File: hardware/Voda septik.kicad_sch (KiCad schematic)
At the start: 39 parts, among them J1 Screw_Terminal_01x09, J2 RS-485 elektroměr, J3 Display TM1637, J4 Display LCD I2C, U1 ESP32-DevKitC, U2 DC-DC 24V -> 5V, U4 MAX3485-modul

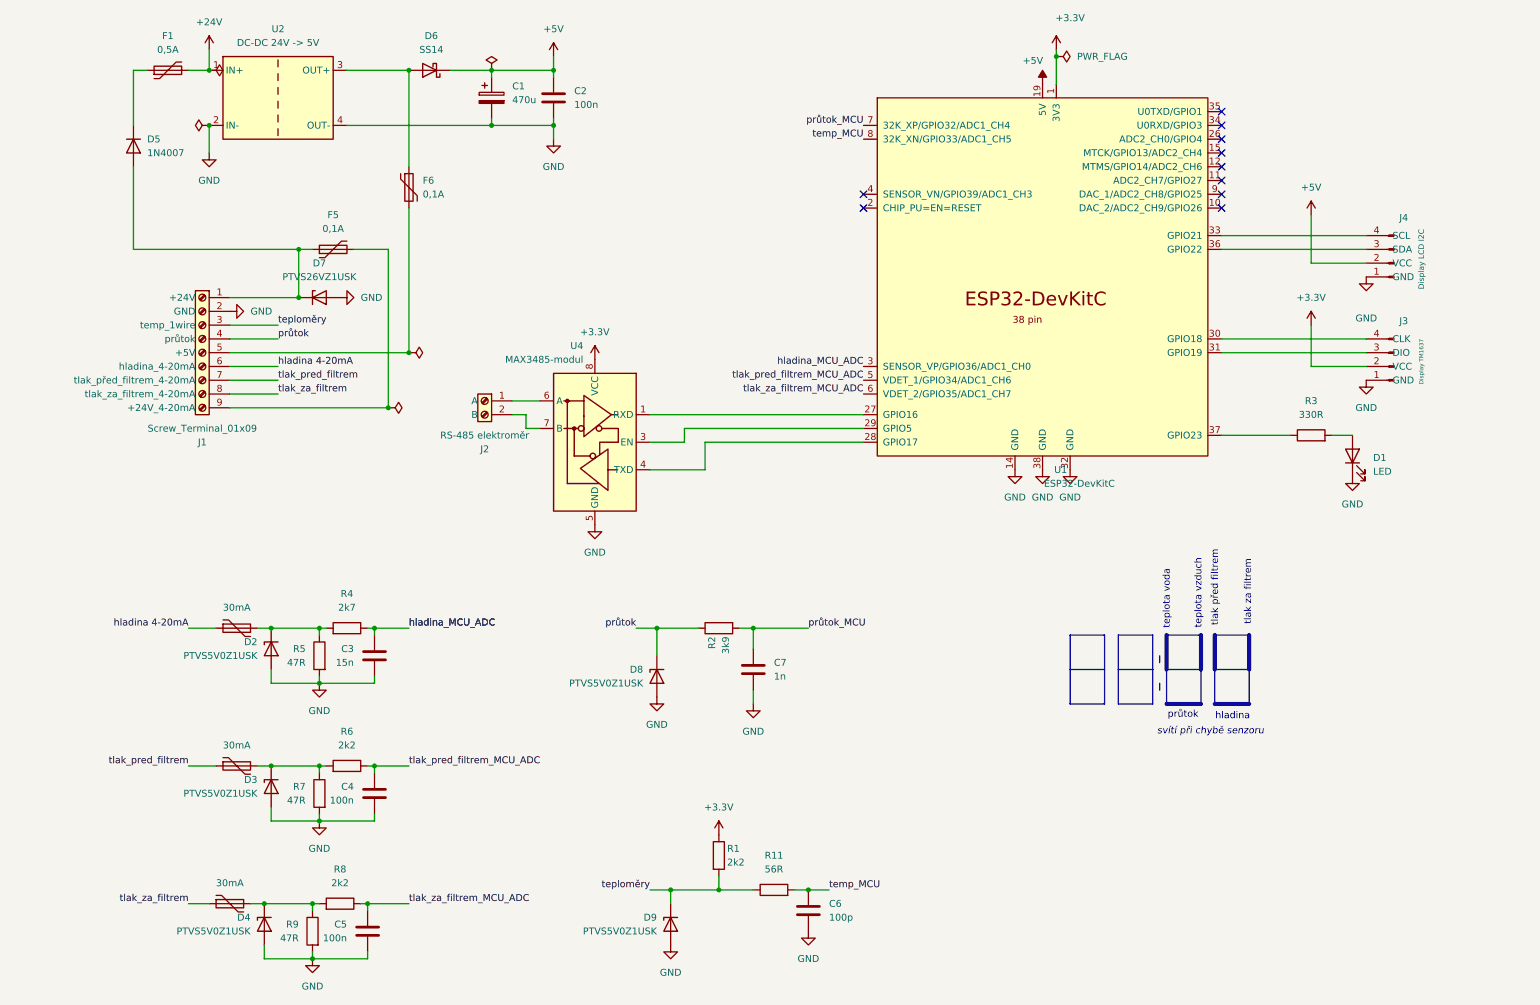
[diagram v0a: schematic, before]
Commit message: Dokončení schématu a návrhu PCB o stavu, který byl poslán do výroby.
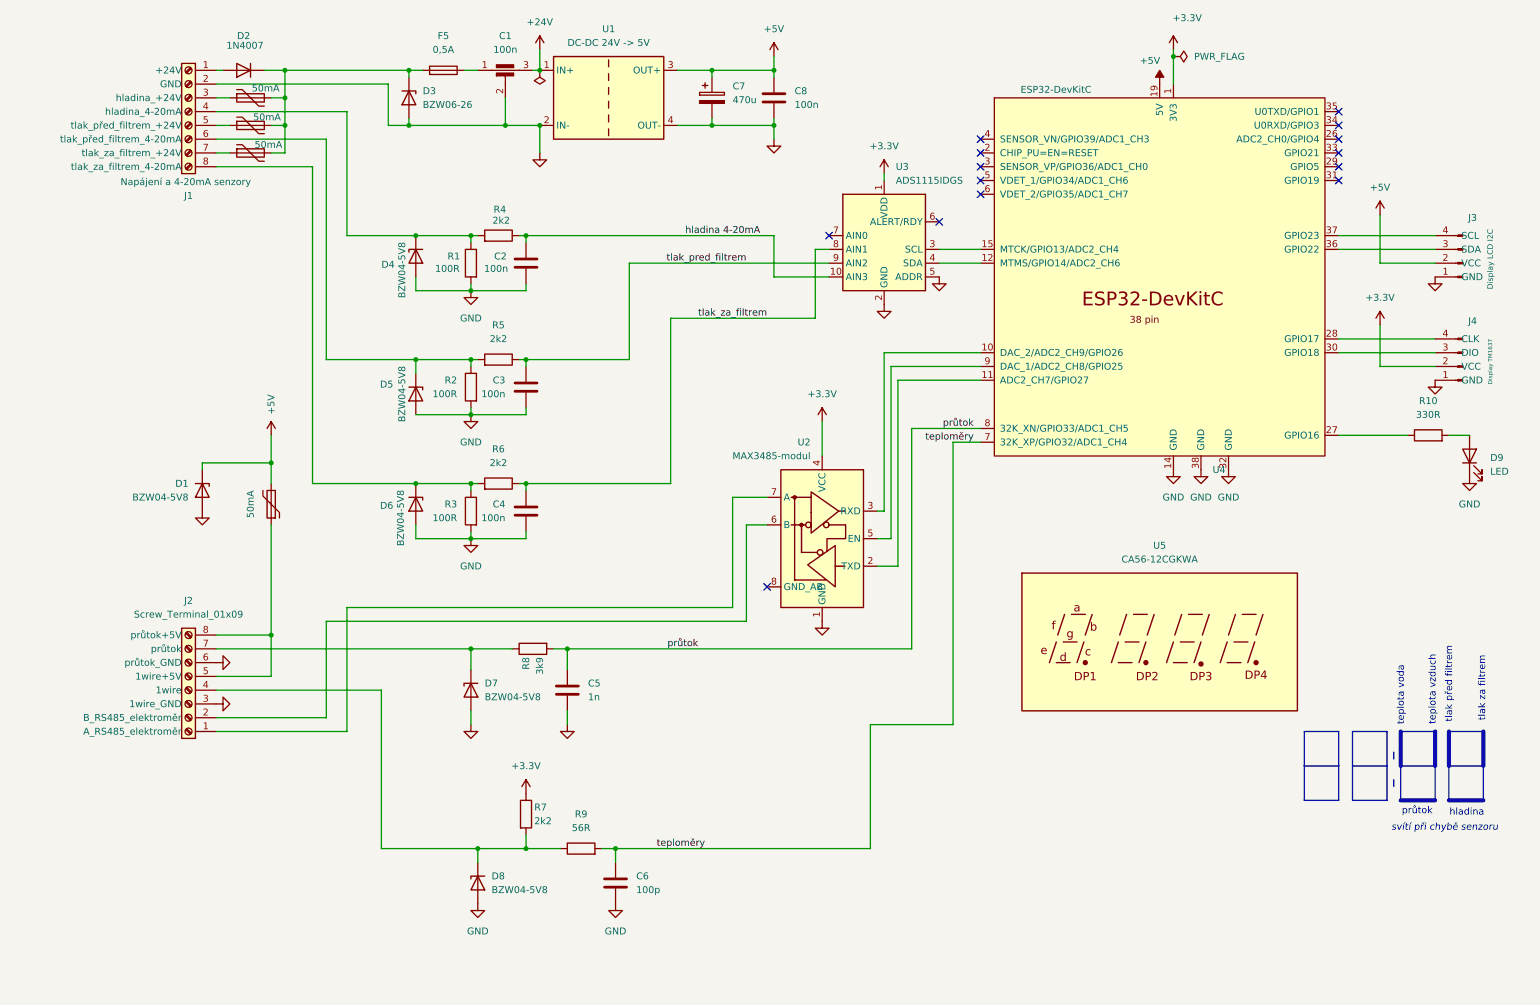
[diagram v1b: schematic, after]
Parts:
- removed D3, D4: PTVS5V0Z1USK, Diode_SMD:Nexperia_DSN1608-2_1.6x0.8mm, symbol Diode:PTVS5V0Z1USK
- removed D6: SS14, symbol Device:D_Schottky
- removed F6: 0,1A, symbol Device:Polyfuse
- removed J2: RS-485 elektroměr, TerminalBlock_RND:TerminalBlock_RND_205-00001_1x02_P5.00mm_Horizontal, symbol Connector:Screw_Terminal_01x02
- added C1: 100n, martin:Odruseni_3x_2.54mm, symbol Device:Filter_EMI_C
- added D1, D5, D6: BZW04-5V8, Diode_THT:D_DO-15_P2.54mm_Vertical_AnodeUp, symbol martin:BZW04-5V8
- added J2: Screw_Terminal_01x09, martin:Svorky_EB147A_8_5.08, symbol Connector:Screw_Terminal_01x09
- added U3: ADS1115IDGS, martin:ADS1115_modul_vertical, symbol Analog_ADC:ADS1115IDGS
- added U5: CA56-12CGKWA, martin:DISPLAY_clok_MOUNT_4xM3, symbol Display_Character:CA56-12CGKWA
- C2: renamed from C3; value 15n -> 100n; footprint (none) -> Capacitor_THT:C_Disc_D5.0mm_W2.5mm_P5.00mm
- C3: renamed from C4; footprint (none) -> Capacitor_THT:C_Disc_D5.0mm_W2.5mm_P5.00mm
- C4: renamed from C5; footprint (none) -> Capacitor_THT:C_Disc_D5.0mm_W2.5mm_P5.00mm
- C5: renamed from C7; footprint (none) -> Capacitor_THT:C_Disc_D5.0mm_W2.5mm_P5.00mm
- C6: footprint (none) -> Capacitor_THT:C_Disc_D5.0mm_W2.5mm_P5.00mm
- C7: renamed from C1; footprint (none) -> Capacitor_THT:CP_Radial_D10.0mm_P5.00mm
- C8: renamed from C2; footprint (none) -> Capacitor_THT:C_Disc_D5.0mm_W2.5mm_P5.00mm
- D2: renamed from D5; footprint Diode_THT:D_DO-41_SOD81_P10.16mm_Horizontal -> Diode_THT:D_DO-15_P2.54mm_Vertical_AnodeUp
- D3: renamed from D7; value PTVS26VZ1USK -> BZW06-26; footprint Diode_SMD:Nexperia_DSN1608-2_1.6x0.8mm -> Diode_THT:D_DO-15_P2.54mm_Vertical_AnodeUp; symbol Diode:PTVS26VZ1USK -> martin:BZW06-26
- D4: renamed from D2; value PTVS5V0Z1USK -> BZW04-5V8; footprint Diode_SMD:Nexperia_DSN1608-2_1.6x0.8mm -> Diode_THT:D_DO-15_P2.54mm_Vertical_AnodeUp; symbol Diode:PTVS5V0Z1USK -> martin:BZW04-5V8
- D7: renamed from D8; value PTVS5V0Z1USK -> BZW04-5V8; footprint Diode_SMD:Nexperia_DSN1608-2_1.6x0.8mm -> Diode_THT:D_DO-15_P2.54mm_Vertical_AnodeUp; symbol Diode:PTVS5V0Z1USK -> martin:BZW04-5V8
- D8: renamed from D9; value PTVS5V0Z1USK -> BZW04-5V8; footprint Diode_SMD:Nexperia_DSN1608-2_1.6x0.8mm -> Diode_THT:D_DO-15_P2.54mm_Vertical_AnodeUp; symbol Diode:PTVS5V0Z1USK -> martin:BZW04-5V8
- D9: renamed from D1; footprint (none) -> LED_THT:LED_D3.0mm
- F1: renamed from F2; value 30mA -> 50mA; footprint (none) -> martin:Fuse_Disc_D8.3_W3.8_P5.1
- F2: renamed from F3; value 30mA -> 50mA; footprint (none) -> martin:Fuse_Disc_D8.3_W3.8_P5.1
- F3: renamed from F4; value 30mA -> 50mA; footprint (none) -> martin:Fuse_Disc_D8.3_W3.8_P5.1
- F4: renamed from F5; value 0,1A -> 50mA; footprint (none) -> martin:Fuse_Disc_D8.3_W3.8_P5.1
- F5: renamed from F1; footprint (none) -> martin:Fuse_Axial_L11mm_D3.9mm_P15.24mm_Horizontal
- J1: value Screw_Terminal_01x09 -> Napájení a 4-20mA senzory; footprint TerminalBlock_Phoenix:TerminalBlock_Phoenix_MKDS-1,5-9_1x09_P5.00mm_Horizontal -> martin:Svorky_EB147A_8_5.08
- J3: renamed from J4; footprint (none) -> Connector_PinHeader_2.54mm:PinHeader_1x04_P2.54mm_Vertical
- J4: renamed from J3; footprint (none) -> Connector_PinHeader_2.54mm:PinHeader_1x04_P2.54mm_Vertical
- R1: renamed from R5; value 47R -> 100R; footprint (none) -> Resistor_THT:R_Axial_DIN0207_L6.3mm_D2.5mm_P2.54mm_Vertical
- R10: renamed from R3; footprint (none) -> Resistor_THT:R_Axial_DIN0207_L6.3mm_D2.5mm_P2.54mm_Vertical
- R2: renamed from R7; value 47R -> 100R; footprint (none) -> Resistor_THT:R_Axial_DIN0207_L6.3mm_D2.5mm_P2.54mm_Vertical
- R3: renamed from R9; value 47R -> 100R; footprint (none) -> Resistor_THT:R_Axial_DIN0207_L6.3mm_D2.5mm_P2.54mm_Vertical
- R4: value 2k7 -> 2k2; footprint (none) -> Resistor_THT:R_Axial_DIN0207_L6.3mm_D2.5mm_P2.54mm_Vertical
- R5: renamed from R6; footprint (none) -> Resistor_THT:R_Axial_DIN0207_L6.3mm_D2.5mm_P2.54mm_Vertical
- R6: renamed from R8; footprint (none) -> Resistor_THT:R_Axial_DIN0207_L6.3mm_D2.5mm_P2.54mm_Vertical
- R7: renamed from R1; footprint (none) -> Resistor_THT:R_Axial_DIN0207_L6.3mm_D2.5mm_P2.54mm_Vertical
- R8: renamed from R2; footprint (none) -> Resistor_THT:R_Axial_DIN0207_L6.3mm_D2.5mm_P2.54mm_Vertical
- R9: renamed from R11; footprint (none) -> Resistor_THT:R_Axial_DIN0207_L6.3mm_D2.5mm_P2.54mm_Vertical
- U1: renamed from U2; footprint Converter_DCDC:Converter_DCDC_Murata_CRE1xxxxxxDC_THT -> martin:LM2596 DC-DC HW-411
- U2: renamed from U4; footprint (none) -> martin:MAX3485-modul
- renumbered U1 to U4
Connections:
- net +24V: now also C1.3; no longer F5.2
- net +3.3V: now also U2.4 (VCC), U3.1 (VDD); no longer U2.8 (VCC)
- net +5V: now also F4.2, U1.3 (OUT+), D1.1 (K)
- net GND: now also U2.1 (GND), C1.2, D1.2 (A), D5.2 (A), D6.2 (A), J2.3 (1wire_GND), J2.6 (průtok_GND), U3.2 (GND), U3.5 (ADDR); no longer U2.5 (GND)
- net hladina 4-20mA: now also C2.1, R4.1, U3.10 (AIN3); no longer F1.1, J1.6 (hladina_4-20mA)
- net průtok: now also C5.1, R8.2, U4.8 (32K_XN/GPIO33/ADC1_CH5); no longer D7.1 (K), J1.4 (průtok), R8.1
- net teploměry: now also C6.1, R9.2, U4.7 (32K_XP/GPIO32/ADC1_CH4); no longer D8.1 (K), J1.3 (temp_1wire), R7.2, R9.1
- net tlak_pred_filtrem: now also C3.1, R5.1, U3.9 (AIN2); no longer F2.1, J1.7 (tlak_před_filtrem_4-20mA)
- net tlak_za_filtrem: now also C4.1, R6.1, U3.8 (AIN1); no longer F3.1, J1.8 (tlak_za_filtrem_4-20mA)
- net at D2.1 (K), F5.1: now also D3.1 (K), F1.2, F2.2, F3.2
- net at R2.1, R5.2: now also J1.6 (tlak_před_filtrem_4-20mA), D5.1 (K); no longer F2.2
- net at R10.1: now also U4.27 (GPIO16); no longer U4.37 (GPIO23)
- net at D4.1 (K), R1.1, R4.2: now also J1.4 (hladina_4-20mA); no longer F1.2
- net at J4.3 (DIO): now also U4.30 (GPIO18); no longer U4.31 (GPIO19)
- net at J4.4 (CLK): now also U4.28 (GPIO17); no longer U4.30 (GPIO18)
- net at J1.5 (tlak_před_filtrem_+24V): now also F2.1
- net at U2.3 (RXD): now also U4.10 (DAC_2/ADC2_CH9/GPIO26); no longer U4.29 (GPIO5)
- net at U2.6 (B): now also J2.2 (B_RS485_elektroměr)
- net at U2.7 (A): now also J2.1 (A_RS485_elektroměr)
- net at R3.1, R6.2: now also J1.8 (tlak_za_filtrem_4-20mA), D6.1 (K); no longer F3.2
- net at U4.11 (ADC2_CH7/GPIO27): now also U2.2 (TXD)
- net at U4.12 (MTMS/GPIO14/ADC2_CH6): now also U3.4 (SDA)
- net at U4.15 (MTCK/GPIO13/ADC2_CH4): now also U3.3 (SCL)
- net at U4.33 (GPIO21): no longer J3.4 (SCL)
- net at U4.9 (DAC_1/ADC2_CH8/GPIO25): now also U2.5 (EN)
- net at D2.2 (A), J1.1 (+24V): no longer D3.1 (K), F4.1
- removed net hladina_MCU_ADC: C2.1, R4.1, U4.3 (SENSOR_VP/GPIO36/ADC1_CH0)
- removed net průtok_MCU: C5.1, R8.2, U4.7 (32K_XP/GPIO32/ADC1_CH4)
- removed net temp_MCU: C6.1, R9.2, U4.8 (32K_XN/GPIO33/ADC1_CH5)
- removed net tlak_pred_filtrem_MCU_ADC: C3.1, R5.1, U4.5 (VDET_1/GPIO34/ADC1_CH6)
- removed net tlak_za_filtrem_MCU_ADC: C4.1, R6.1, U4.6 (VDET_2/GPIO35/ADC1_CH7)
- new net: C1.1, F5.2
- new net: D8.1 (K), J2.4 (1wire), R7.2, R9.1
- new net: D7.1 (K), J2.7 (průtok), R8.1
- new net: F3.1, J1.7 (tlak_za_filtrem_+24V)
- new net: J3.4 (SCL), U4.37 (GPIO23)
- new net: F1.1, J1.3 (hladina_+24V)
- new net: F4.1, J2.5 (1wire+5V), J2.8 (průtok+5V)
- no-connect marks 10 -> 14
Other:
- moved on the sheet: C2, C3, C4, C5, C6, C7, C8, D2, D3, D4, D7, D8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
